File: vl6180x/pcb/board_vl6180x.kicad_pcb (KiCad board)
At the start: 2 copper layers, 45.5 x 19 mm, 21 parts, among them P1 CONN_6, Q1 BSS138, Q2 BSS138, U1 LP3985IM5

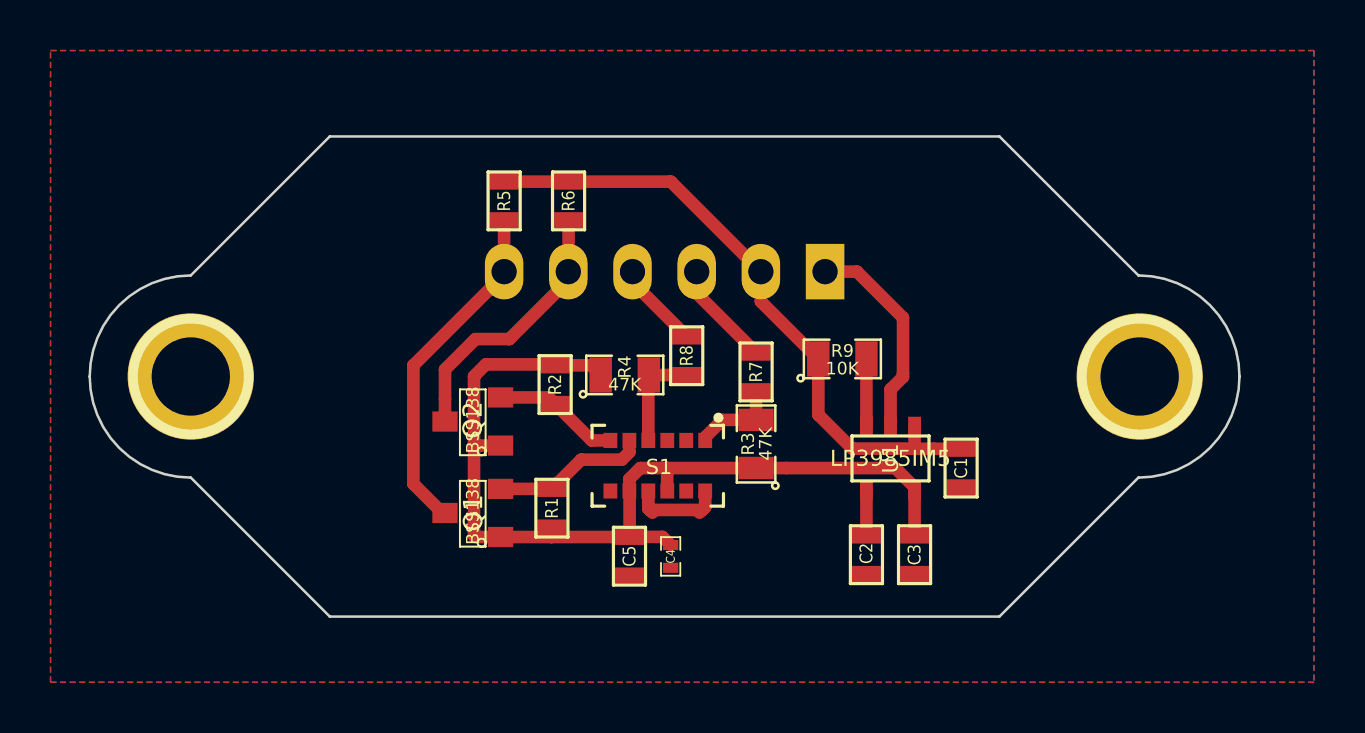
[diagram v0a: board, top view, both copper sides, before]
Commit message: rerouting tracks and utilization of my own libraries
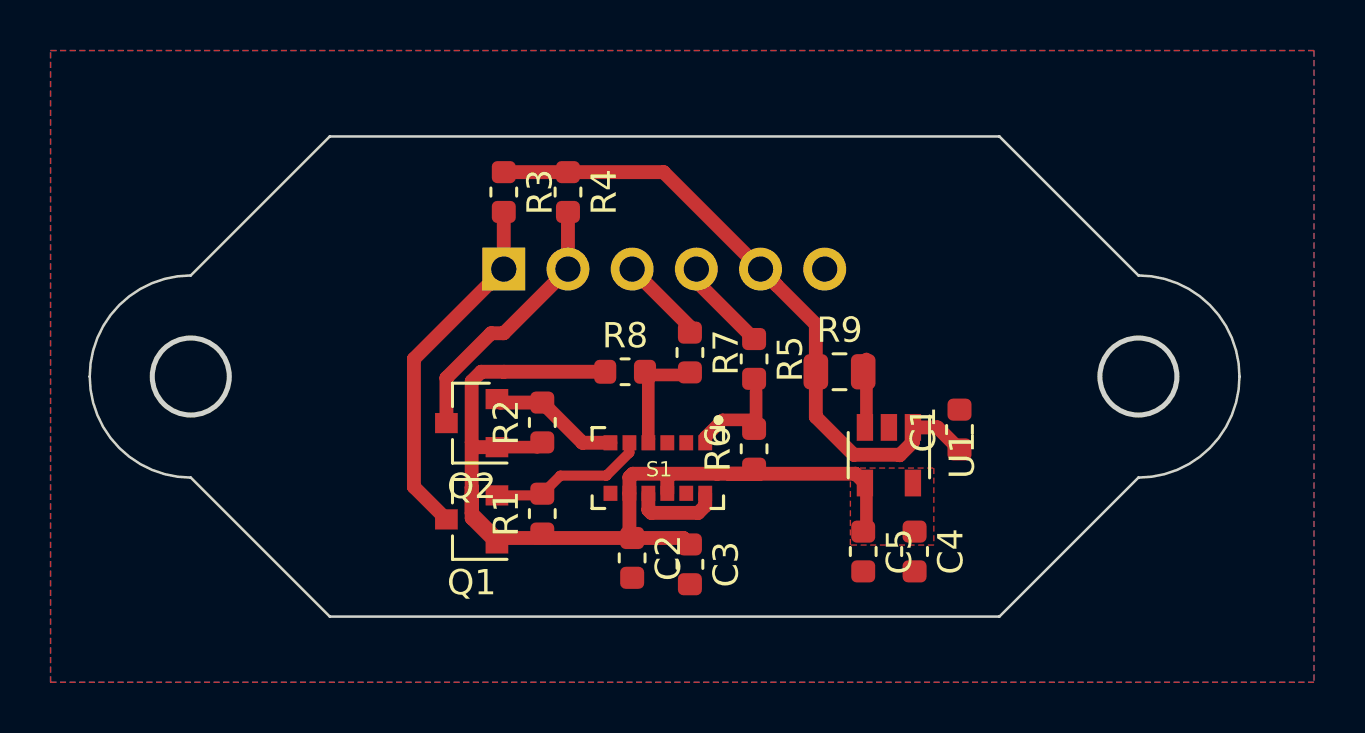
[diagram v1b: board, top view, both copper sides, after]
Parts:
- removed 1PIN (x2): P***, connect:1pin
- removed P1: CONN_6, w_pin_strip:pin_strip_6-90
- added J1: Conn_01x06, Connector_PinHeader_2.54mm:PinHeader_1x06_P2.54mm_Horizontal, B.Cu at (150.2, 68.6)
- C1: footprint libcms:SM0603 -> Resistor_SMD:R_0603_1608Metric
- C2: value 1uF -> 100nF; footprint libcms:SM0603 -> Resistor_SMD:R_0603_1608Metric
- C3: value 1uF -> 4.7uF; footprint libcms:SM0603 -> Resistor_SMD:R_0603_1608Metric
- C4: value 100nF -> 1uF; footprint libcms:SM0402 -> Resistor_SMD:R_0603_1608Metric
- C5: value 4.7uF -> 1uF; footprint libcms:SM0603 -> Resistor_SMD:R_0603_1608Metric
- Q1, Q2: footprint libcms:SOT23 -> Package_TO_SOT_SMD:SOT-23
- R1, R2: value 2K2 -> 2k2; footprint libcms:SM0603 -> Resistor_SMD:R_0603_1608Metric
- R3, R4: value 47K -> 2k2; footprint libcms:SM0805 -> Resistor_SMD:R_0603_1608Metric
- R5: value 2K2 -> 10k; footprint libcms:SM0603 -> Resistor_SMD:R_0603_1608Metric
- R6: value 2K2 -> 47k; footprint libcms:SM0603 -> Resistor_SMD:R_0603_1608Metric
- R7: value 10K -> 10k; footprint libcms:SM0603 -> Resistor_SMD:R_0603_1608Metric
- R8: value 10K -> 47k; footprint libcms:SM0603 -> Resistor_SMD:R_0603_1608Metric
- R9: value 10K -> 10k; footprint libcms:SM0805 -> Resistor_SMD:R_0805_2012Metric
- S1: value VL6180X -> ST_VL6180X; footprint myfootprint:ST_VL6180X -> dodo-custom-ics:ST_VL6180X
- U1: value LP3985IM5 -> LD3985M28R; footprint libcms:SOT23-5 -> Package_TO_SOT_SMD:SOT-23-5
- moved R3 14.1 mm to (150.2, 65.6), turned to -90 degrees
- moved R6 12.3 mm to (160.2, 75.7)
- moved R5 11.7 mm to (160.2, 72.2), turned to -90 degrees
- moved C4 9.65 mm to (166.5, 79.8)
- moved C2 9.27 mm to (155.3, 80.0), turned to -90 degrees
- moved C5 9.25 mm to (164.5, 79.8)
- moved C3 8.90 mm to (157.6, 80.3), turned to -90 degrees
- moved R4 7.58 mm to (152.8, 65.6), turned to -90 degrees
- moved R7 2.73 mm to (157.6, 71.9), turned to -90 degrees
- moved R8 2.52 mm to (155.0, 72.7), turned to 0 degrees
- moved R2 1.58 mm to (151.8, 74.7)
- moved C1 1.53 mm to (168.3, 75.0)
- moved R9 0.52 mm to (163.5, 72.7)
- moved R1 0.44 mm to (151.8, 78.3), turned to 90 degrees
- moved Q1 0.26 mm to (149.0, 78.5), turned to 180 degrees
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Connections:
- C1 pad 1: GND -> +5V
- C1 pad 2: +5V -> GNDD
- C2 pad 1: GND -> +2V8
- C2 pad 2: Net-(C2-Pad2) -> GNDD
- C3 pad 1: GND -> +2V8
- C3 pad 2: +2V8 -> GNDD
- C4 pad 2: GND -> GNDD
- C5 pad 2: GND -> GNDD
- Q1 pad 2: SCL_LW -> /SCL_LW
- Q1 pad 3: I2C_SCL -> /SCL_HG
- Q2 pad 2: SDA_LW -> /SDA_LW
- Q2 pad 3: I2C_SDA -> /SDA_HG
- R1 pad 1: SCL_LW -> +2V8
- R1 pad 2: +2V8 -> /SCL_LW
- R2 pad 1: SDA_LW -> +2V8
- R2 pad 2: +2V8 -> /SDA_LW
- R3 pad 1: +2V8 -> +5V
- R3 pad 2: Net-(R3-Pad2) -> /SCL_HG
- R4 pad 1: +2V8 -> +5V
- R4 pad 2: Net-(R4-Pad2) -> /SDA_HG
- R5 pad 1: I2C_SCL -> /IO_1
- R5 pad 2: +5V -> Net-(R5-Pad2)
- R6 pad 1: I2C_SDA -> +2V8
- R6 pad 2: +5V -> Net-(R5-Pad2)
- R7 pad 1: Net-(R3-Pad2) -> /IO_0
- R7 pad 2: IO_1 -> Net-(R7-Pad2)
- R8 pad 1: Net-(R4-Pad2) -> +2V8
- R8 pad 2: IO_0 -> Net-(R7-Pad2)
- S1 pad 1: Net-(R3-Pad2) -> Net-(R5-Pad2)
- S1 pad 11: Net-(S1-Pad11) -> (no net)
- S1 pad 12: GND -> GNDD
- S1 pad 2: Net-(S1-Pad2) -> (no net)
- S1 pad 3: Net-(S1-Pad3) -> (no net)
- S1 pad 4: Net-(R4-Pad2) -> Net-(R7-Pad2)
- S1 pad 5: SCL_LW -> /SCL_LW
- S1 pad 6: SDA_LW -> /SDA_LW
- S1 pad 7: Net-(S1-Pad7) -> (no net)
- S1 pad 9: GND -> GNDD
- U1 pad 2: GND -> (no net)
- U1 pad 4: Net-(C2-Pad2) -> +2V8
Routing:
- net /SCL_HG: track 0.00 -> 14.2 mm
- net I2C_SCL: track 13.7 -> 0.00 mm
- net GND: track 12.5 -> 0.00 mm
- net I2C_SDA: track 11.3 -> 0.00 mm
- net /SDA_HG: track 0.00 -> 11.1 mm
- net SCL_LW: track 6.42 -> 0.00 mm
- net /SCL_LW: track 0.00 -> 6.33 mm
- net /SDA_LW: track 0.00 -> 5.21 mm
- net SDA_LW: track 5.05 -> 0.00 mm
- net IO_1: track 4.21 -> 0.00 mm
- net Net-(R7-Pad2): track 0.00 -> 4.10 mm
- net Net-(R4-Pad2): track 4.10 -> 0.00 mm
- net /IO_1: track 0.00 -> 3.72 mm
- net IO_0: track 3.66 -> 0.00 mm
- net GNDD: track 0.00 -> 3.57 mm
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- added copper zone on F.Cu, net +2V8
- added copper zone on B.Cu, net GNDD
- added copper zone on F.Cu, net GNDD
- removed copper zone on B.Cu, net GND
- removed copper zone on F.Cu, net GND
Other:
- outline, holes or cut-outs redrawn
- net class Default removed
